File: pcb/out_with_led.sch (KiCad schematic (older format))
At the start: 2 parts

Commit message: Update
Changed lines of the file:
@@
 AR Path="/5C24272E/5C245D08/5C2454EF" Ref="R63"  Part="1"
 AR Path="/5C24272E/5C245D0C/5C2454EF" Ref="R64"  Part="1"
-F 0 "R33" V 3243 4050 50  0000 C CNN
+F 0 "R64" V 3243 4050 50  0000 C CNN
 F 1 "1k" V 3334 4050 50  0000 C CNN
 F 2 "Resistor_THT:R_Axial_DIN0207_L6.3mm_D2.5mm_P7.62mm_Horizontal" V 3380 4050 50  0001 C CNN
@@
 AR Path="/5C24272E/5C245D08/5C2455CB" Ref="D63"  Part="1"
 AR Path="/5C24272E/5C245D0C/5C2455CB" Ref="D64"  Part="1"
-F 0 "D33" H 2992 3795 50  0000 C CNN
+F 0 "D64" H 2992 3795 50  0000 C CNN
 F 1 "RED" H 2992 3886 50  0000 C CNN
 F 2 "LED_THT:LED_D3.0mm" H 3000 4050 50  0001 C CNN

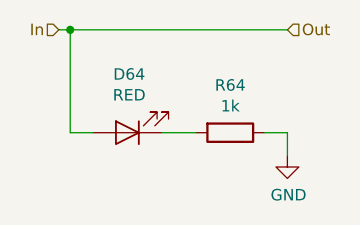
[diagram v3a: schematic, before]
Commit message: Changed some footprints, spacing out components
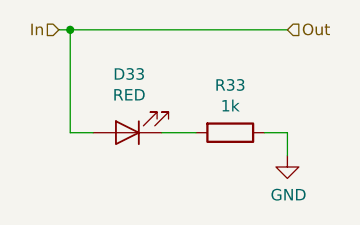
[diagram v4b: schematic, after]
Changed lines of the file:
@@
 AR Path="/5C24272E/5C245D08/5C2454EF" Ref="R63"  Part="1"
 AR Path="/5C24272E/5C245D0C/5C2454EF" Ref="R64"  Part="1"
-F 0 "R64" V 3243 4050 50  0000 C CNN
+F 0 "R33" V 3243 4050 50  0000 C CNN
 F 1 "1k" V 3334 4050 50  0000 C CNN
 F 2 "Resistor_THT:R_Axial_DIN0207_L6.3mm_D2.5mm_P7.62mm_Horizontal" V 3380 4050 50  0001 C CNN
@@
 AR Path="/5C24272E/5C245D08/5C2455CB" Ref="D63"  Part="1"
 AR Path="/5C24272E/5C245D0C/5C2455CB" Ref="D64"  Part="1"
-F 0 "D64" H 2992 3795 50  0000 C CNN
+F 0 "D33" H 2992 3795 50  0000 C CNN
 F 1 "RED" H 2992 3886 50  0000 C CNN
 F 2 "LED_THT:LED_D3.0mm" H 3000 4050 50  0001 C CNN
